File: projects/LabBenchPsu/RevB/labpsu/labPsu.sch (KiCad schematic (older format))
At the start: 44 parts, among them IC5 LM358, K1 CONN_3, K2 CONN_3, P1 Screw terminal, P2 CONN_1, P3 CONN_1, P4 CONN_1, P5 CONN_1, P6 CONN_2, P7 CONN_2, Q4 PN2222, Q5 PN2222, U1 AZ1117, U2 MCP4725, U3 ISL21070, U4 32u4ProtoFeather

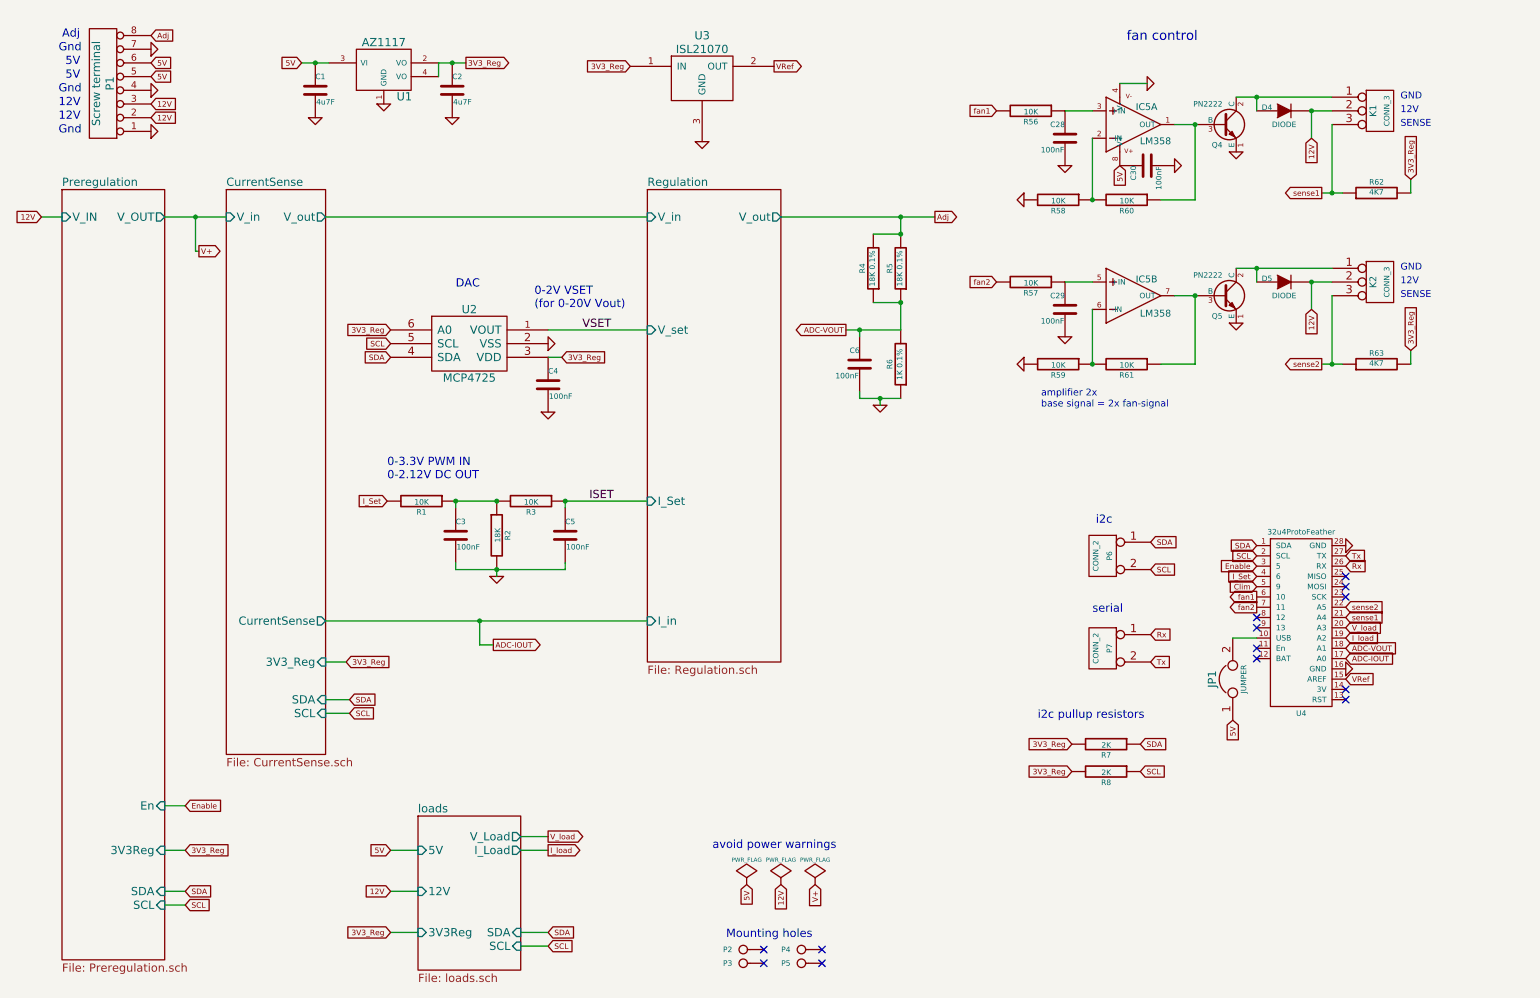
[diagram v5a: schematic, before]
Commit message: schematic with new DAC
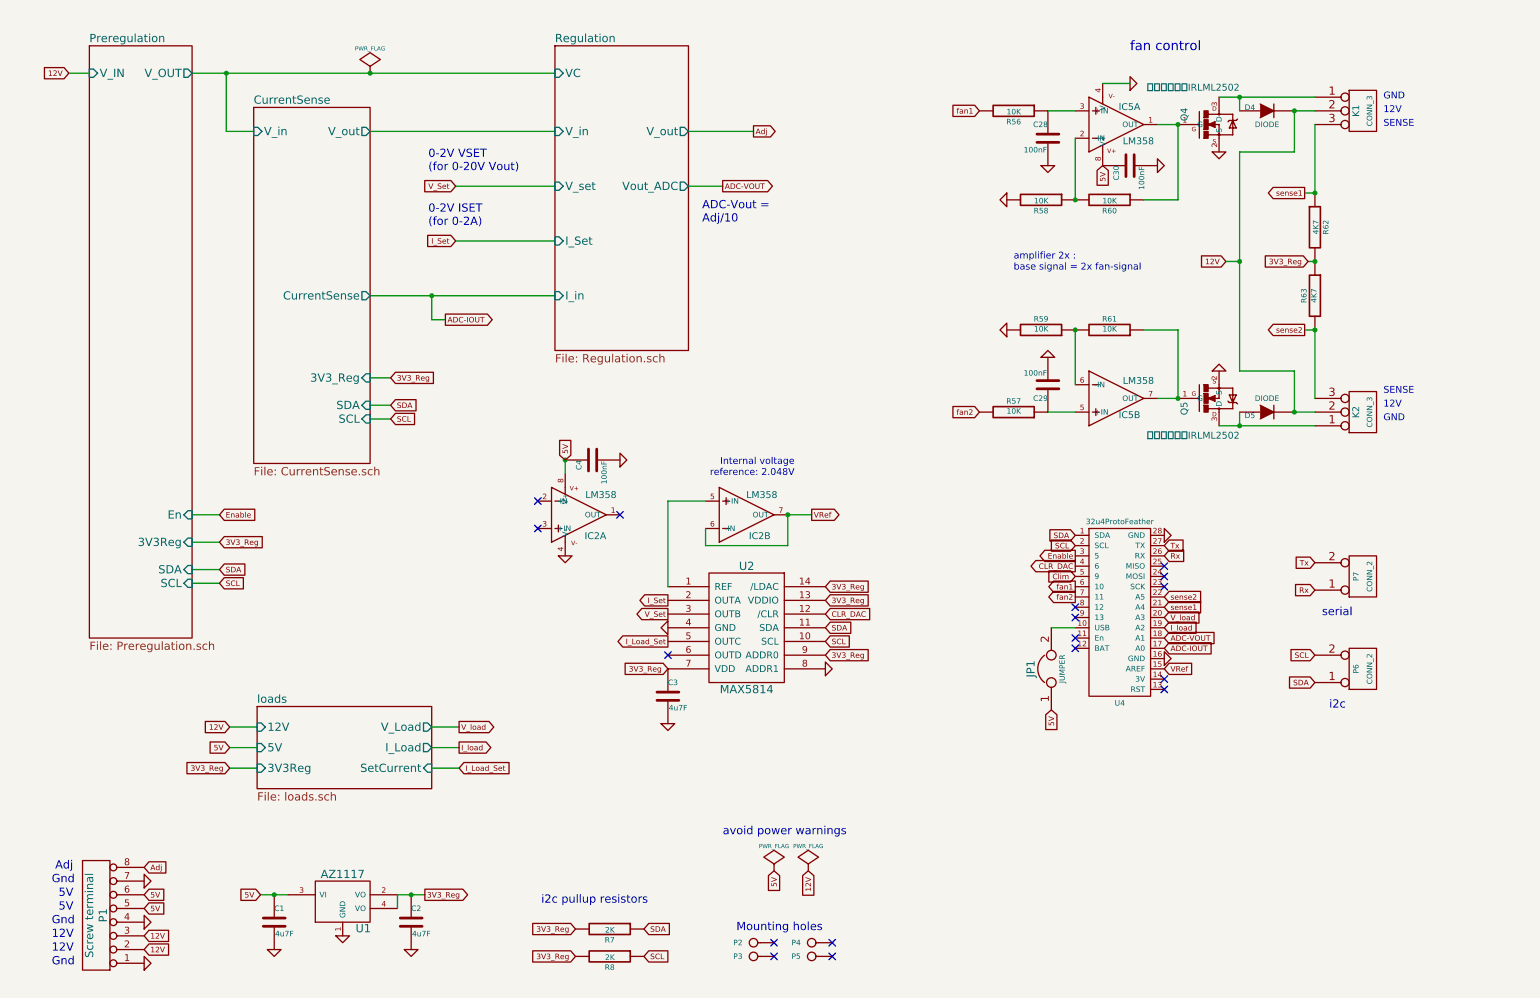
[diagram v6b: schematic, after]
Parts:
- removed C5, C6: 100nF, symbol C
- removed Q4, Q5: PN2222, symbol 2N3904
- removed R1, R3: 10K, symbol R
- removed R2: 18K, symbol R
- removed R4, R5: 18K 0.1%, symbol R
- removed R6: 1K 0.1%, symbol R
- removed U2: MCP4725, symbol MCP4725
- removed U3: ISL21070, symbol ISL21070
- added IC2: LM358, symbol OPAMP-DUALU
- added Q4, Q5: IRLML2502, symbol MOSFET-N
- added U2: MAX5814, symbol MAX5814
- C3: value 100nF -> 4u7F
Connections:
- net 3V3_Reg: now also C3.1, R63.1, U2.13 (VDDIO), U2.14 (/LDAC), U2.7 (VDD), U2.9 (ADDR0); no longer C4.1, R63.2
- net 5V: now also C4.1, IC2.8 (V+)
- net GND: now also IC2.4 (V-), Q4.2 (S), Q5.2 (S), U2.4 (GND), U2.8 (ADDR1)
- net I_Set: now also U2.2 (OUTA); no longer U4.4 (6)
- net SCL: now also U2.10 (SCL)
- net SDA: now also U2.11 (SDA)
- net VRef: now also IC2.6 (-IN), IC2.7 (OUT)
- net sense2: now also R63.2; no longer R63.1
- net at IC5.1 (OUT), R60.1: now also Q4.1 (G)
- net at IC5.7 (OUT), R61.1: now also Q5.1 (G)
- net at D4.1 (A), K1.1 (P1): now also Q4.3 (D)
- net at D5.1 (A), K2.1 (P1): now also Q5.3 (D)
- new net: IC2.5 (+IN), U2.1 (REF)
- new net CLR_DAC: U2.12 (/CLR), U4.4 (6)
- new net I_Load_Set: U2.5 (OUTC)
- new net V_Set: U2.3 (OUTB)
- no-connect marks 13 -> 17
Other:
- note added: "0-2V ISET \n(for 0-2A)"
- note added: "ADC-Vout =\nAdj/10"
- note added: "Internal voltage \nreference: 2.048V"
- note added: "amplifier 2x :\nbase signal = 2x fan-signal"
- note removed: "0-3.3V PWM IN\n0-2.12V DC OUT"
- note removed: "DAC"
- note removed: "amplifier 2x\nbase signal = 2x fan-signal"
- moved on the sheet: C1, C2, C28, C29, C30, D4, D5, IC5A, IC5B, JP1, K1, K2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

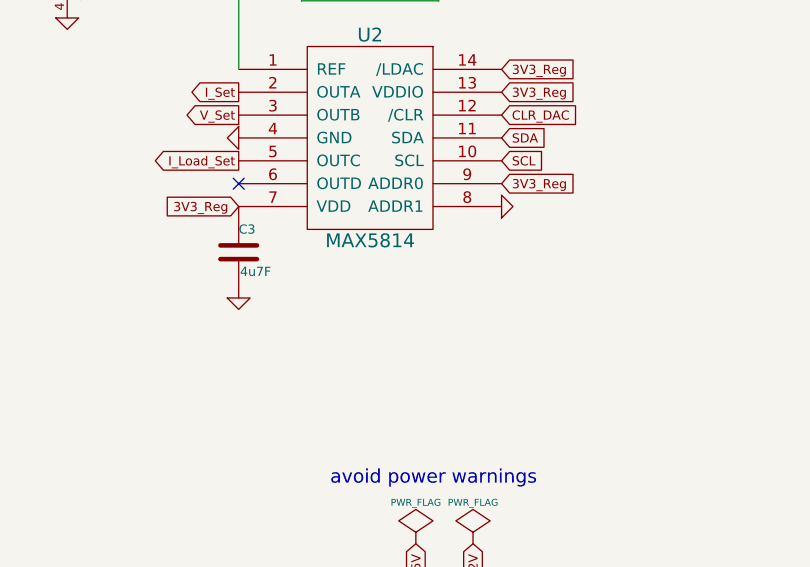
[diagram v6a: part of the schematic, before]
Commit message: i2c addresses added
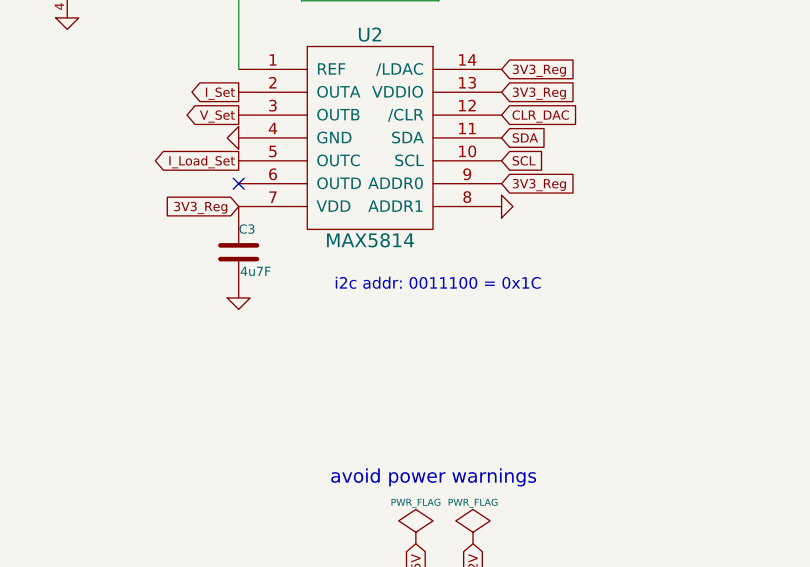
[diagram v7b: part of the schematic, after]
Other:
- note added: "i2c addr: 0011100 = 0x1C"
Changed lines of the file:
@@
 	9450 3250 9850 3250
 Connection ~ 9450 2450
+Text Notes 6600 5800 2    50   ~ 0
+i2c addr: 0011100 = 0x1C
 $EndSCHEMATC

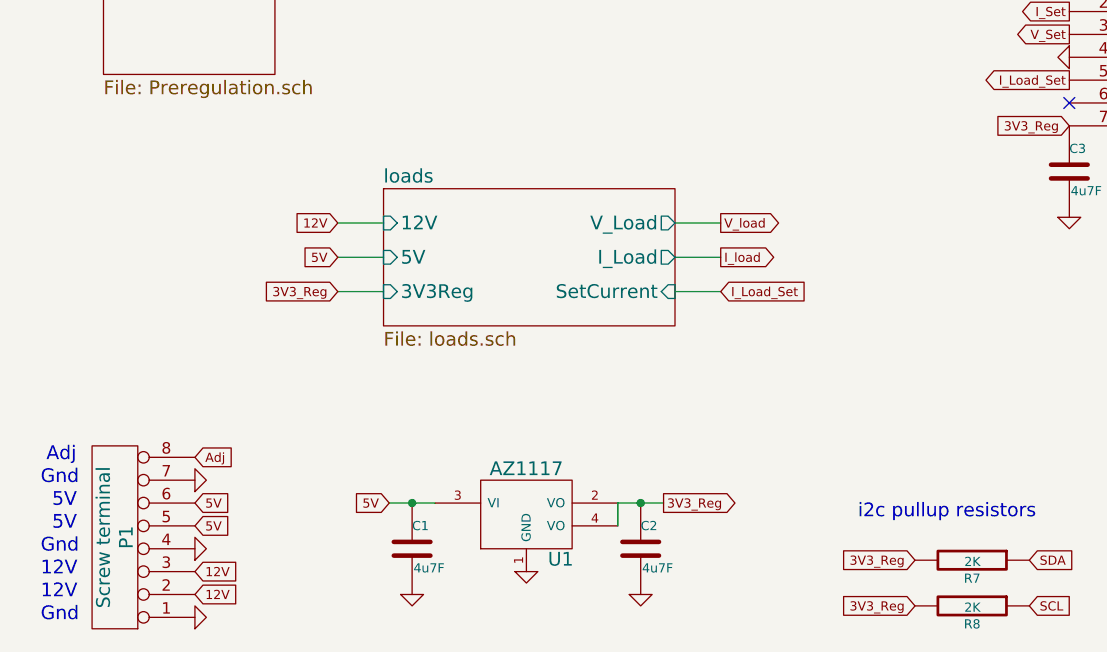
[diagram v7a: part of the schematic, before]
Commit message: sepic calculations added
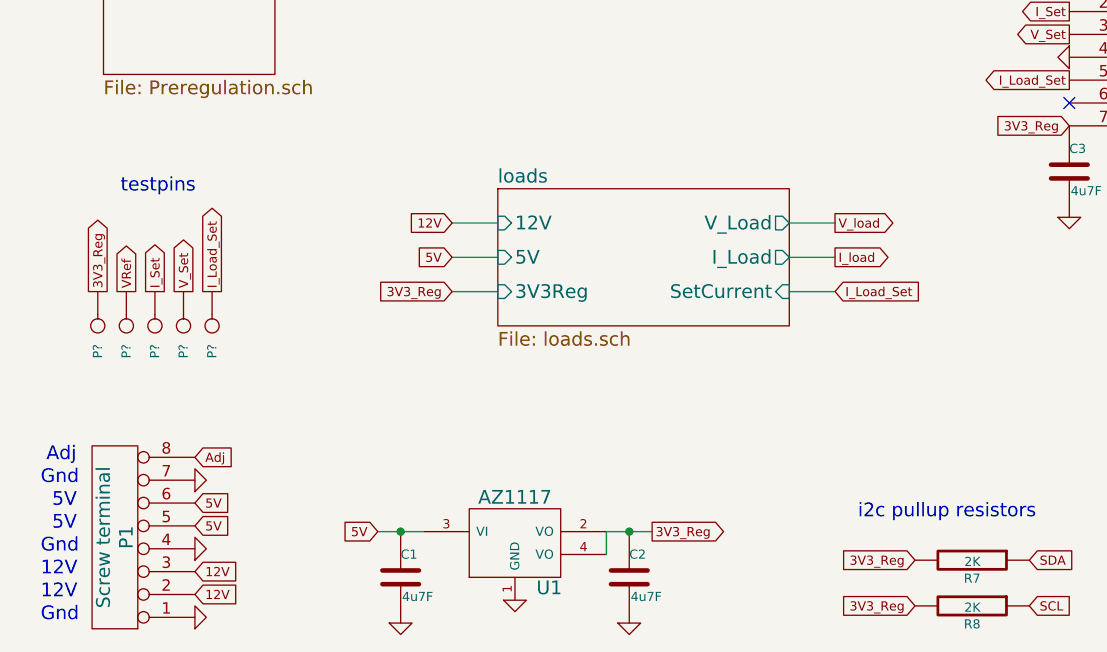
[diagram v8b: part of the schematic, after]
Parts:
- added P? (x5): CONN_1, frep:MountingHole_3mm, symbol CONN_1
- JP1: footprint (none) -> frep:Pin_Proto_Straight_1x02
- K1, K2: footprint (none) -> frep:Pin_Proto_Straight_1x03
- P1: footprint (none) -> frep:terminal_3p5mm_8pin
- P2, P3, P4, P5: footprint (none) -> frep:MountingHole_3mm
- U1: footprint (none) -> frep:SOT223
- U4: footprint (none) -> frep:feather
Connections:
- net 3V3_Reg: now also P?.1
- net I_Load_Set: now also P?.1
- net I_Set: now also P?.1
- net VRef: now also P?.1
- net V_Set: now also P?.1
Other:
- note added: "testpins"
- moved on the sheet: C1, C2, U1
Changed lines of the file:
@@
 F 0 "P1" V 1050 7225 60  0000 C CNN
 F 1 "Screw terminal" V 1150 7225 60  0000 C CNN
-F 2 "" H 1100 7225 60  0001 C CNN
+F 2 "frep:terminal_3p5mm_8pin" H 1100 7225 60  0001 C CNN
 F 3 "" H 1100 7225 60  0000 C CNN
 	1    1100 7225
@@
 F 0 "P3" H 5980 7525 40  0000 L CNN
 F 1 "CONN_1" H 5900 7580 30  0001 C CNN
-F 2 "" H 5900 7525 60  0001 C CNN
+F 2 "frep:MountingHole_3mm" H 5900 7525 60  0001 C CNN
 F 3 "" H 5900 7525 60  0000 C CNN
 	1    5900 7525
@@
 F 0 "P2" H 5980 7425 40  0000 L CNN
 F 1 "CONN_1" H 5900 7480 30  0001 C CNN
-F 2 "" H 5900 7425 60  0001 C CNN
+F 2 "frep:MountingHole_3mm" H 5900 7425 60  0001 C CNN
 F 3 "" H 5900 7425 60  0000 C CNN
 	1    5900 7425
@@
 F 0 "P5" H 6405 7525 40  0000 L CNN
 F 1 "CONN_1" H 6325 7580 30  0001 C CNN
-F 2 "" H 6325 7525 60  0001 C CNN
+F 2 "frep:MountingHole_3mm" H 6325 7525 60  0001 C CNN
 F 3 "" H 6325 7525 60  0000 C CNN
 	1    6325 7525
@@
 F 0 "P4" H 6405 7425 40  0000 L CNN
 F 1 "CONN_1" H 6325 7480 30  0001 C CNN
-F 2 "" H 6325 7425 60  0001 C CNN
+F 2 "frep:MountingHole_3mm" H 6325 7425 60  0001 C CNN
 F 3 "" H 6325 7425 60  0000 C CNN
 	1    6325 7425
@@
 L AZ1117 U1
 U 1 1 57DD5F0A
-P 2900 7125
-F 0 "U1" H 3050 6929 60  0000 C CNN
-F 1 "AZ1117" H 2900 7325 60  0000 C CNN
-F 2 "" H 2900 7125 60  0001 C CNN
-F 3 "" H 2900 7125 60  0000 C CNN
-	1    2900 7125
+P 2850 7250
+F 0 "U1" H 3000 7054 60  0000 C CNN
+F 1 "AZ1117" H 2850 7450 60  0000 C CNN
+F 2 "frep:SOT223" H 2850 7250 60  0001 C CNN
+F 3 "" H 2850 7250 60  0000 C CNN
+	1    2850 7250
 	1    0    0    -1
 $EndComp
@@
 L C C1
 U 1 1 57DD6110
-P 2400 7275
-F 0 "C1" H 2400 7375 40  0000 L CNN
-F 1 "4u7F" H 2406 7190 40  0000 L CNN
-F 2 "" H 2438 7125 30  0001 C CNN
-F 3 "" H 2400 7275 60  0000 C CNN
-	1    2400 7275
+P 2350 7400
+F 0 "C1" H 2350 7500 40  0000 L CNN
+F 1 "4u7F" H 2356 7315 40  0000 L CNN
+F 2 "" H 2388 7250 30  0001 C CNN
+F 3 "" H 2350 7400 60  0000 C CNN
+	1    2350 7400
 	1    0    0    -1
 $EndComp
@@
 L C C2
 U 1 1 57DD61A7
-P 3400 7275
-F 0 "C2" H 3400 7375 40  0000 L CNN
-F 1 "4u7F" H 3406 7190 40  0000 L CNN
-F 2 "" H 3438 7125 30  0001 C CNN
-F 3 "" H 3400 7275 60  0000 C CNN
-	1    3400 7275
+P 3350 7400
+F 0 "C2" H 3350 7500 40  0000 L CNN
+F 1 "4u7F" H 3356 7315 40  0000 L CNN
+F 2 "" H 3388 7250 30  0001 C CNN
+F 3 "" H 3350 7400 60  0000 C CNN
+	1    3350 7400
 	1    0    0    -1
 $EndComp
@@
 L GND #PWR03
 U 1 1 57DD63A5
-P 2400 7475
-F 0 "#PWR03" H 2400 7475 30  0001 C CNN
-F 1 "GND" H 2400 7405 30  0001 C CNN
-F 2 "" H 2400 7475 60  0000 C CNN
-F 3 "" H 2400 7475 60  0000 C CNN
-	1    2400 7475
+P 2350 7600
+F 0 "#PWR03" H 2350 7600 30  0001 C CNN
+F 1 "GND" H 2350 7530 30  0001 C CNN
+F 2 "" H 2350 7600 60  0000 C CNN
+F 3 "" H 2350 7600 60  0000 C CNN
+	1    2350 7600
 	1    0    0    -1
 $EndComp
@@
 L GND #PWR04
 U 1 1 57DD645A
-P 2900 7375
-F 0 "#PWR04" H 2900 7375 30  0001 C CNN
-F 1 "GND" H 2900 7305 30  0001 C CNN
-F 2 "" H 2900 7375 60  0000 C CNN
-F 3 "" H 2900 7375 60  0000 C CNN
-	1    2900 7375
+P 2850 7500
+F 0 "#PWR04" H 2850 7500 30  0001 C CNN
+F 1 "GND" H 2850 7430 30  0001 C CNN
+F 2 "" H 2850 7500 60  0000 C CNN
+F 3 "" H 2850 7500 60  0000 C CNN
+	1    2850 7500
 	1    0    0    -1
 $EndComp
@@
 L GND #PWR05
 U 1 1 57DD64A7
-P 3400 7475
-F 0 "#PWR05" H 3400 7475 30  0001 C CNN
-F 1 "GND" H 3400 7405 30  0001 C CNN
-F 2 "" H 3400 7475 60  0000 C CNN
-F 3 "" H 3400 7475 60  0000 C CNN
-	1    3400 7475
-	1    0    0    -1
-$EndComp
-Text GLabel 2300 7075 0    40   Input ~ 0
+P 3350 7600
+F 0 "#PWR05" H 3350 7600 30  0001 C CNN
+F 1 "GND" H 3350 7530 30  0001 C CNN
+F 2 "" H 3350 7600 60  0000 C CNN
+F 3 "" H 3350 7600 60  0000 C CNN
+	1    3350 7600
+	1    0    0    -1
+$EndComp
+Text GLabel 2250 7200 0    40   Input ~ 0
 5V
 Text GLabel 2000 4500 2    40   Input ~ 0
@@
 F 0 "U4" H 8575 4425 40  0000 C CNN
 F 1 "32u4ProtoFeather" H 8575 5750 40  0000 C CNN
-F 2 "" H 8575 5275 40  0001 C CNN
+F 2 "frep:feather" H 8575 5275 40  0001 C CNN
 F 3 "" H 8575 5275 40  0000 C CNN
 	1    8575 5050
@@
 F 0 "JP1" H 8075 5575 60  0000 C CNN
 F 1 "JUMPER" H 8075 5345 40  0000 C CNN
-F 2 "" H 8075 5425 60  0001 C CNN
+F 2 "frep:Pin_Proto_Straight_1x02" H 8075 5425 60  0001 C CNN
 F 3 "" H 8075 5425 60  0000 C CNN
 	1    8075 5425
@@
 Text GLabel 8900 5425 2    40   Input ~ 0
 VRef
-Text GLabel 3500 7075 2    40   Output ~ 0
+Text GLabel 3450 7200 2    40   Output ~ 0
 3V3_Reg
 NoConn ~ 8250 4975
@@
 5V
 $Sheet
-S 2275 5700 1275 600
+S 2775 5700 1275 600
 U 57E1BFC0
 F0 "loads" 60
 F1 "loads.sch" 60
-F2 "5V" I L 2275 6000 60
-F3 "12V" I L 2275 5850 60
-F4 "V_Load" O R 3550 5850 60
-F5 "I_Load" O R 3550 6000 60
-F6 "3V3Reg" I L 2275 6150 60
-F7 "SetCurrent" I R 3550 6150 60
+F2 "5V" I L 2775 6000 60
+F3 "12V" I L 2775 5850 60
+F4 "V_Load" O R 4050 5850 60
+F5 "I_Load" O R 4050 6000 60
+F6 "3V3Reg" I L 2775 6150 60
+F7 "SetCurrent" I R 4050 6150 60
 $EndSheet
-Text GLabel 2075 6000 0    40   Input ~ 0
+Text GLabel 2575 6000 0    40   Input ~ 0
 5V
-Text GLabel 2075 5850 0    40   Input ~ 0
+Text GLabel 2575 5850 0    40   Input ~ 0
 12V
 $Sheet
@@
 NoConn ~ 8900 4750
 NoConn ~ 8900 4825
-Text GLabel 3750 5850 2    40   Output ~ 0
+Text GLabel 4250 5850 2    40   Output ~ 0
 V_load
-Text GLabel 3750 6000 2    40   Output ~ 0
+Text GLabel 4250 6000 2    40   Output ~ 0
 I_load
 Text GLabel 8900 5050 2    40   Input ~ 0
@@
 F 0 "K2" V 10300 3550 50  0000 C CNN
 F 1 "CONN_3" V 10400 3550 40  0000 C CNN
-F 2 "" H 10350 3550 60  0001 C CNN
+F 2 "frep:Pin_Proto_Straight_1x03" H 10350 3550 60  0001 C CNN
 F 3 "" H 10350 3550 60  0000 C CNN
 	1    10350 3550
@@
 F 0 "K1" V 10300 1350 50  0000 C CNN
 F 1 "CONN_3" V 10400 1350 40  0000 C CNN
-F 2 "" H 10350 1350 60  0001 C CNN
+F 2 "frep:Pin_Proto_Straight_1x03" H 10350 1350 60  0001 C CNN
 F 3 "" H 10350 1350 60  0000 C CNN
 	1    10350 1350
@@
 Text Notes 6200 4025 2    50   ~ 0
 Internal voltage \nreference: 2.048V
-Text GLabel 2075 6150 0    40   Input ~ 0
+Text GLabel 2575 6150 0    40   Input ~ 0
 3V3_Reg
-Text GLabel 3750 6150 2    40   Input ~ 0
+Text GLabel 4250 6150 2    40   Input ~ 0
 I_Load_Set
 Text GLabel 4525 3900 1    40   Input ~ 0
@@
 ADC-Vout =\nAdj/10
 Wire Wire Line
-	2300 7075 2500 7075
-Connection ~ 2400 7075
-Wire Wire Line
-	3300 7175 3300 7075
-Wire Wire Line
-	3300 7075 3500 7075
-Connection ~ 3400 7075
+	2250 7200 2450 7200
+Connection ~ 2350 7200
+Wire Wire Line
+	3250 7300 3250 7200
+Wire Wire Line
+	3250 7200 3450 7200
+Connection ~ 3350 7200
 Wire Wire Line
 	900  1075 1050 1075
@@
 Connection ~ 2050 1075
 Wire Wire Line
-	2075 6000 2275 6000
-Wire Wire Line
-	2075 5850 2275 5850
+	2575 6000 2775 6000
+Wire Wire Line
+	2575 5850 2775 5850
 Wire Wire Line
 	3650 2875 3550 2875
@@
 	5425 1500 5900 1500
 Wire Wire Line
-	3550 5850 3750 5850
-Wire Wire Line
-	3550 6000 3750 6000
+	4050 5850 4250 5850
+Wire Wire Line
+	4050 6000 4250 6000
 Wire Wire Line
 	8450 1150 8650 1150
@@
 Connection ~ 6150 4300
 Wire Wire Line
-	2075 6150 2275 6150
-Wire Wire Line
-	3750 6150 3550 6150
+	2575 6150 2775 6150
+Wire Wire Line
+	4250 6150 4050 6150
 Connection ~ 4525 3900
 Wire Wire Line
@@
 Text Notes 6600 5800 2    50   ~ 0
 i2c addr: 0011100 = 0x1C
+Text Notes 1125 5725 0    60   ~ 0
+testpins
+$Comp
+L CONN_1 P?
+U 1 1 581FA728
+P 1025 6300
+F 0 "P?" H 1105 6300 40  0000 L CNN
+F 1 "CONN_1" H 1025 6355 30  0001 C CNN
+F 2 "frep:MountingHole_3mm" H 1025 6300 60  0001 C CNN
+F 3 "" H 1025 6300 60  0000 C CNN
+	1    1025 6300
+	0    1    1    0
+$EndComp
+Text GLabel 1025 6150 1    40   Output ~ 0
+3V3_Reg
+$Comp
+L CONN_1 P?
+U 1 1 581FADB1
+P 1150 6300
+F 0 "P?" H 1230 6300 40  0000 L CNN
+F 1 "CONN_1" H 1150 6355 30  0001 C CNN
+F 2 "frep:MountingHole_3mm" H 1150 6300 60  0001 C CNN
+F 3 "" H 1150 6300 60  0000 C CNN
+	1    1150 6300
+	0    1    1    0
+$EndComp
+Text GLabel 1150 6150 1    40   Output ~ 0
+VRef
+$Comp
+L CONN_1 P?
+U 1 1 581FB3F4
+P 1275 6300
+F 0 "P?" H 1355 6300 40  0000 L CNN
+F 1 "CONN_1" H 1275 6355 30  0001 C CNN
+F 2 "frep:MountingHole_3mm" H 1275 6300 60  0001 C CNN
+F 3 "" H 1275 6300 60  0000 C CNN
+	1    1275 6300
+	0    1    1    0
+$EndComp
+$Comp
+L CONN_1 P?
+U 1 1 581FB516
+P 1400 6300
+F 0 "P?" H 1480 6300 40  0000 L CNN
+F 1 "CONN_1" H 1400 6355 30  0001 C CNN
+F 2 "frep:MountingHole_3mm" H 1400 6300 60  0001 C CNN
+F 3 "" H 1400 6300 60  0000 C CNN
+	1    1400 6300
+	0    1    1    0
+$EndComp
+$Comp
+L CONN_1 P?
+U 1 1 581FB63B
+P 1525 6300
+F 0 "P?" H 1605 6300 40  0000 L CNN
+F 1 "CONN_1" H 1525 6355 30  0001 C CNN
+F 2 "frep:MountingHole_3mm" H 1525 6300 60  0001 C CNN
+F 3 "" H 1525 6300 60  0000 C CNN
+	1    1525 6300
+	0    1    1    0
+$EndComp
+Text GLabel 1275 6150 1    40   Output ~ 0
+I_Set
+Text GLabel 1400 6150 1    40   Output ~ 0
+V_Set
+Text GLabel 1525 6150 1    40   Output ~ 0
+I_Load_Set
 $EndSCHEMATC
